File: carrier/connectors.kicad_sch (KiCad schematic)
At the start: 1 part, among them J11 Conn_02x05_Top_Bottom

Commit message: Fix: relinked footprints
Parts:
- added J12: Conn_02x40_Odd_Even, symbol Connector_Generic:Conn_02x40_Odd_Even
- J11: footprint (none) -> Connector_PinHeader_2.54mm:PinHeader_2x05_P2.54mm_Vertical
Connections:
- new net +5v: J12.10 (Pin_10), J12.12 (Pin_12), J12.14 (Pin_14), J12.16 (Pin_16), J12.18 (Pin_18), J12.2 (Pin_2), J12.20 (Pin_20), J12.22 (Pin_22), J12.24 (Pin_24), J12.26 (Pin_26), J12.28 (Pin_28), J12.30 (Pin_30), J12.32 (Pin_32), J12.34 (Pin_34), J12.36 (Pin_36), J12.38 (Pin_38), J12.4 (Pin_4), J12.40 (Pin_40), J12.42 (Pin_42), J12.44 (Pin_44), J12.46 (Pin_46), J12.48 (Pin_48), J12.50 (Pin_50), J12.52 (Pin_52), J12.54 (Pin_54), J12.56 (Pin_56), J12.58 (Pin_58), J12.6 (Pin_6), J12.60 (Pin_60), J12.62 (Pin_62), J12.64 (Pin_64), J12.66 (Pin_66), J12.68 (Pin_68), J12.70 (Pin_70), J12.72 (Pin_72), J12.74 (Pin_74), J12.8 (Pin_8)
- new net GND: J12.11 (Pin_11), J12.13 (Pin_13), J12.15 (Pin_15), J12.17 (Pin_17), J12.19 (Pin_19), J12.21 (Pin_21), J12.23 (Pin_23), J12.25 (Pin_25), J12.27 (Pin_27), J12.29 (Pin_29), J12.31 (Pin_31), J12.33 (Pin_33), J12.35 (Pin_35), J12.37 (Pin_37), J12.39 (Pin_39), J12.41 (Pin_41), J12.43 (Pin_43), J12.45 (Pin_45), J12.47 (Pin_47), J12.49 (Pin_49), J12.51 (Pin_51), J12.53 (Pin_53), J12.55 (Pin_55), J12.57 (Pin_57), J12.59 (Pin_59), J12.61 (Pin_61), J12.63 (Pin_63), J12.65 (Pin_65), J12.67 (Pin_67), J12.69 (Pin_69), J12.71 (Pin_71), J12.73 (Pin_73), J12.75 (Pin_75), J12.9 (Pin_9)
- new net RX: J12.1 (Pin_1), J12.3 (Pin_3)
- new net TX: J12.5 (Pin_5), J12.7 (Pin_7)
- no-connect marks 0 -> 5
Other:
- moved on the sheet: J11

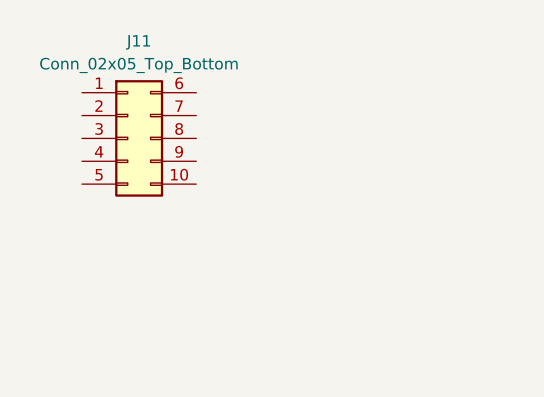
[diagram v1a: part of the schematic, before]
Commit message: Feat: begun work on carrier pcb and imported NGFF m.2 library
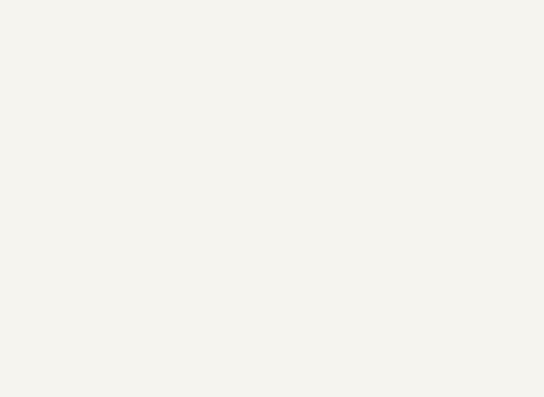
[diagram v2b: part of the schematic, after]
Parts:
- removed J11: Conn_02x05_Top_Bottom, Connector_PinHeader_2.54mm:PinHeader_2x05_P2.54mm_Vertical, symbol Connector_Generic:Conn_02x05_Top_Bottom
- J12: footprint (none) -> M.2:NGFF_A
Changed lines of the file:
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@@
     (effects (font (size 1.27 1.27)) (justify left))
-  )
-  (symbol (lib_id "Connector_Generic:Conn_02x05_Top_Bottom") (at 44.45 59.69 0) (unit 1)
-    (in_bom yes) (on_board yes) (dnp no) (fields_autoplaced)
-    (property "Reference" "J11" (at 45.72 48.895 0)
-      (effects (font (size 1.27 1.27)))
-    )
-    (property "Value" "Conn_02x05_Top_Bottom" (at 45.72 51.435 0)
-      (effects (font (size 1.27 1.27)))
-    )
-    (property "Footprint" "Connector_PinHeader_2.54mm:PinHeader_2x05_P2.54mm_Vertical" (at 44.45 59.69 0)
-      (effects (font (size 1.27 1.27)) hide)
-    )
-    (property "Datasheet" "~" (at 44.45 59.69 0)
-      (effects (font (size 1.27 1.27)) hide)
-    )
-    (pin "1")
-    (pin "10")
-    (pin "2")
-    (pin "3")
-    (pin "4")
-    (pin "5")
-    (pin "6")
-    (pin "7")
-    (pin "8")
-    (pin "9")
-    (instances
-      (project "carrier"
-        (path "/4b1cea9d-93bc-4380-88c3-ede99bb53de2/af6c5568-d2e2-4612-83c1-6e53a7c32d99"
-          (reference "J11") (unit 1)
-        )
-      )
-    )
   )
   (symbol (lib_id "Connector_Generic:Conn_02x40_Odd_Even") (at 111.76 102.235 0) (unit 1)
@@
       (effects (font (size 1.27 1.27)))
     )
-    (property "Footprint" "" (at 111.76 102.235 0)
+    (property "Footprint" "M.2:NGFF_A" (at 111.76 102.235 0)
       (effects (font (size 1.27 1.27)) hide)
     )

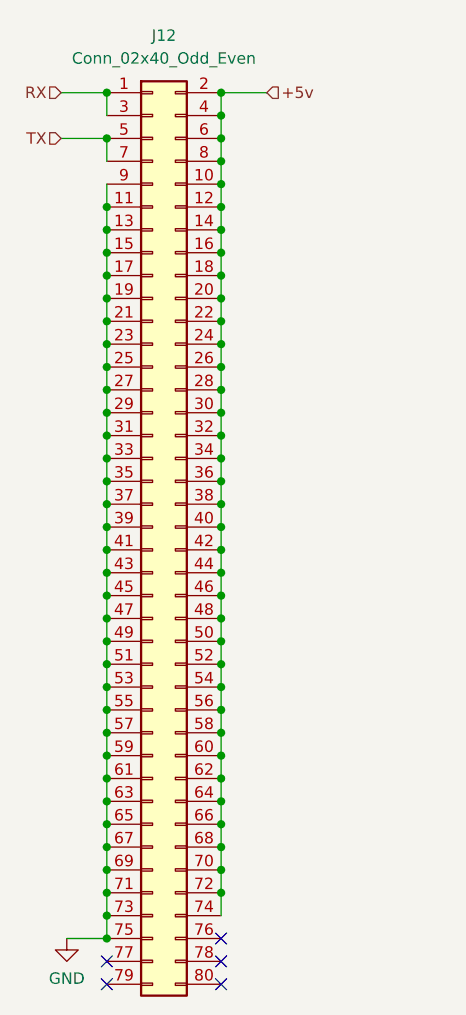
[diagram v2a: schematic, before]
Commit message: Feat: imported m.2 connector and more work on carrier board
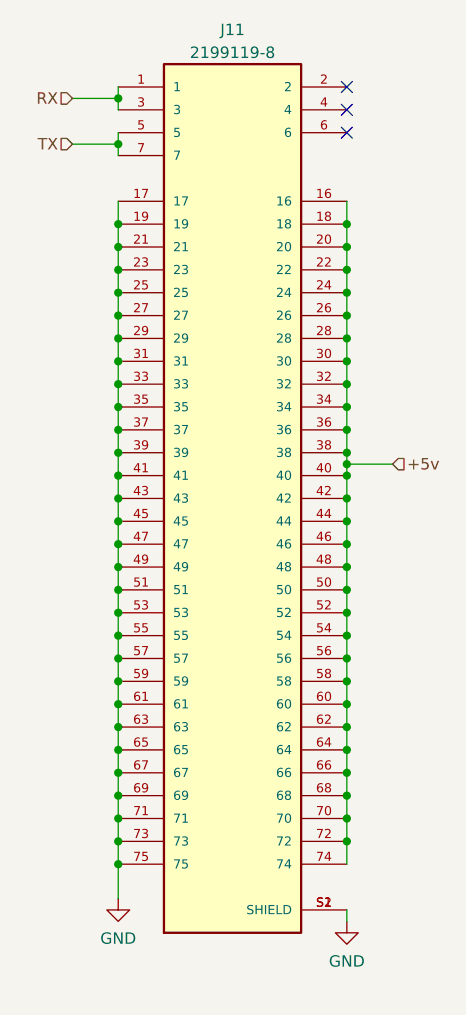
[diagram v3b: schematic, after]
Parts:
- removed J12: Conn_02x40_Odd_Even, M.2:NGFF_A, symbol Connector_Generic:Conn_02x40_Odd_Even
- added J11: 2199119-8, M.2_Connector:TE_2199119-8, symbol M.2_Connector:2199119-8
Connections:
- net +5v: now also J11.16, J11.18, J11.20, J11.22, J11.24, J11.26, J11.28, J11.30, J11.32, J11.34, J11.36, J11.38, J11.40, J11.42, J11.44, J11.46, J11.48, J11.50, J11.52, J11.54, J11.56, J11.58, J11.60, J11.62, J11.64, J11.66, J11.68, J11.70, J11.72, J11.74
- net GND: now also J11.17, J11.19, J11.21, J11.23, J11.25, J11.27, J11.29, J11.31, J11.33, J11.35, J11.37, J11.39, J11.41, J11.43, J11.45, J11.47, J11.49, J11.51, J11.53, J11.55, J11.57, J11.59, J11.61, J11.63, J11.65, J11.67, J11.69, J11.71, J11.73, J11.75, J11.S1 (SHIELD), J11.S2 (SHIELD)
- net RX: now also J11.1, J11.3
- net TX: now also J11.5, J11.7
- no-connect marks 5 -> 3

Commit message: Feat: organized PCB file, preparing for layout and routing.
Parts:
- added J12: Conn_01x04, symbol Connector_Generic:Conn_01x04
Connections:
- net GND: now also J12.2 (Pin_2), J12.4 (Pin_4)
- net RX: now also J12.1 (Pin_1)
- net TX: now also J12.3 (Pin_3)
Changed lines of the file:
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@@
+    (stroke (width 0) (type default))
+  )
+  (wire (pts (xy 163.83 106.68) (xy 170.18 106.68))
     (stroke (width 0) (type default))
   )
@@
     (stroke (width 0) (type default))
   )
+  (wire (pts (xy 163.83 111.76) (xy 170.18 111.76))
+    (stroke (width 0) (type default))
+  )
   (wire (pts (xy 107.95 78.74) (xy 107.95 81.28))
     (stroke (width 0) (type default))
@@
   )
   (hierarchical_label "TX" (shape input) (at 102.87 59.69 180) (fields_autoplaced)
+    (effects (font (size 1.27 1.27)) (justify right))
+  )
+  (hierarchical_label "TX" (shape input) (at 170.18 109.22 180) (fields_autoplaced)
+    (effects (font (size 1.27 1.27)) (justify right))
+  )
+  (hierarchical_label "RX" (shape input) (at 170.18 104.14 180) (fields_autoplaced)
     (effects (font (size 1.27 1.27)) (justify right))
   )
@@
     )
   )
+  (symbol (lib_id "power:GND") (at 163.83 111.76 0) (unit 1)
+    (in_bom yes) (on_board yes) (dnp no)
+    (property "Reference" "#PWR064" (at 163.83 118.11 0)
+      (effects (font (size 1.27 1.27)) hide)
+    )
+    (property "Value" "GND" (at 160.02 113.03 0)
+      (effects (font (size 1.27 1.27)))
+    )
+    (property "Footprint" "" (at 163.83 111.76 0)
+      (effects (font (size 1.27 1.27)) hide)
+    )
+    (property "Datasheet" "" (at 163.83 111.76 0)
+      (effects (font (size 1.27 1.27)) hide)
+    )
+    (pin "1")
+    (instances
+      (project "carrier"
+        (path "/4b1cea9d-93bc-4380-88c3-ede99bb53de2/af6c5568-d2e2-4612-83c1-6e53a7c32d99"
+          (reference "#PWR064") (unit 1)
+        )
+      )
+    )
+  )
   (symbol (lib_id "power:GND") (at 107.95 143.51 0) (unit 1)
     (in_bom yes) (on_board yes) (dnp no) (fields_autoplaced)
@@
     )
   )
+  (symbol (lib_id "Connector_Generic:Conn_01x04") (at 175.26 106.68 0) (unit 1)
+    (in_bom yes) (on_board yes) (dnp no) (fields_autoplaced)
+    (property "Reference" "J12" (at 177.8 107.315 0)
+      (effects (font (size 1.27 1.27)) (justify left))
+    )
+    (property "Value" "Conn_01x04" (at 177.8 109.855 0)
+      (effects (font (size 1.27 1.27)) (justify left))
+    )
+    (property "Footprint" "" (at 175.26 106.68 0)
+      (effects (font (size 1.27 1.27)) hide)
+    )
+    (property "Datasheet" "~" (at 175.26 106.68 0)
+      (effects (font (size 1.27 1.27)) hide)
+    )
+    (pin "1")
+    (pin "2")
+    (pin "3")
+    (pin "4")
+    (instances
+      (project "carrier"
+        (path "/4b1cea9d-93bc-4380-88c3-ede99bb53de2/af6c5568-d2e2-4612-83c1-6e53a7c32d99"
+          (reference "J12") (unit 1)
+        )
+      )
+    )
+  )
   (symbol (lib_id "power:GND") (at 133.35 146.05 0) (unit 1)
     (in_bom yes) (on_board yes) (dnp no) (fields_autoplaced)
@@
         )
       )
+    )
+  )
+  (symbol (lib_id "power:GND") (at 163.83 106.68 0) (unit 1)
+    (in_bom yes) (on_board yes) (dnp no)
+    (property "Reference" "#PWR073" (at 163.83 113.03 0)
+      (effects (font (size 1.27 1.27)) hide)
+    )
+    (property "Value" "GND" (at 160.02 107.95 0)
+      (effects (font (size 1.27 1.27)))
+    )
+    (property "Footprint" "" (at 163.83 106.68 0)
+      (effects (font (size 1.27 1.27)) hide)
+    )
+    (property "Datasheet" "" (at 163.83 106.68 0)
+      (effects (font (size 1.27 1.27)) hide)
+    )
+    (pin "1")
+    (instances
+      (project "carrier"
+        (path "/4b1cea9d-93bc-4380-88c3-ede99bb53de2/af6c5568-d2e2-4612-83c1-6e53a7c32d99"
+          (reference "#PWR073") (unit 1)
+        )
+      )

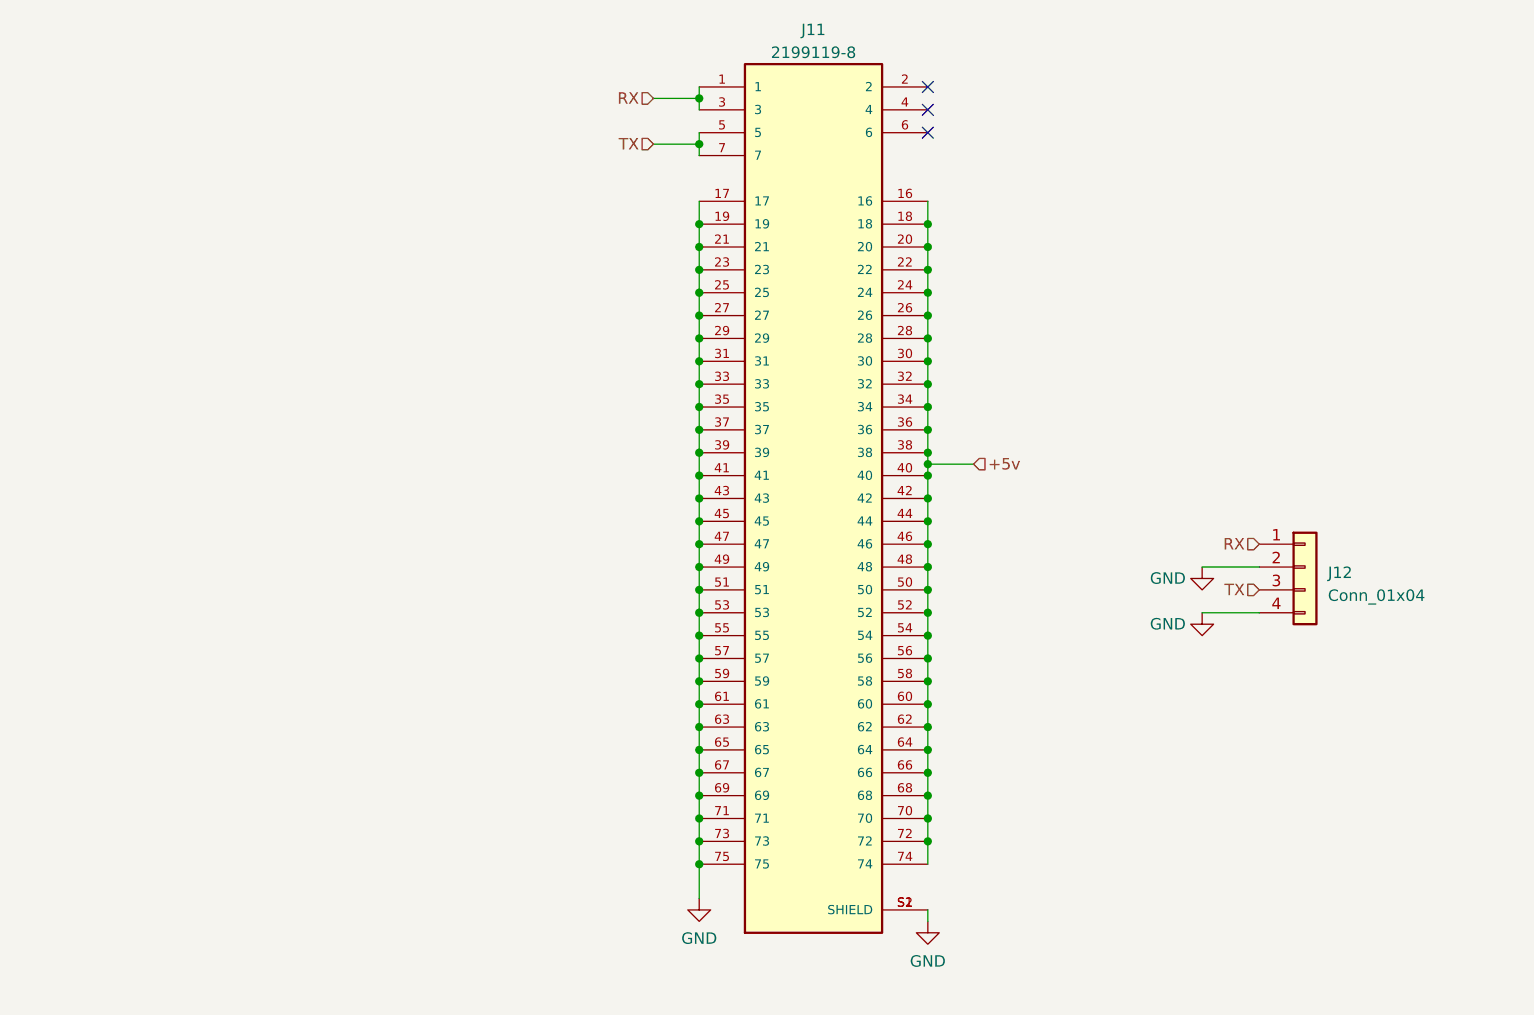
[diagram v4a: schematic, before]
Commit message: Feat: begun work on finalizing PCB layout
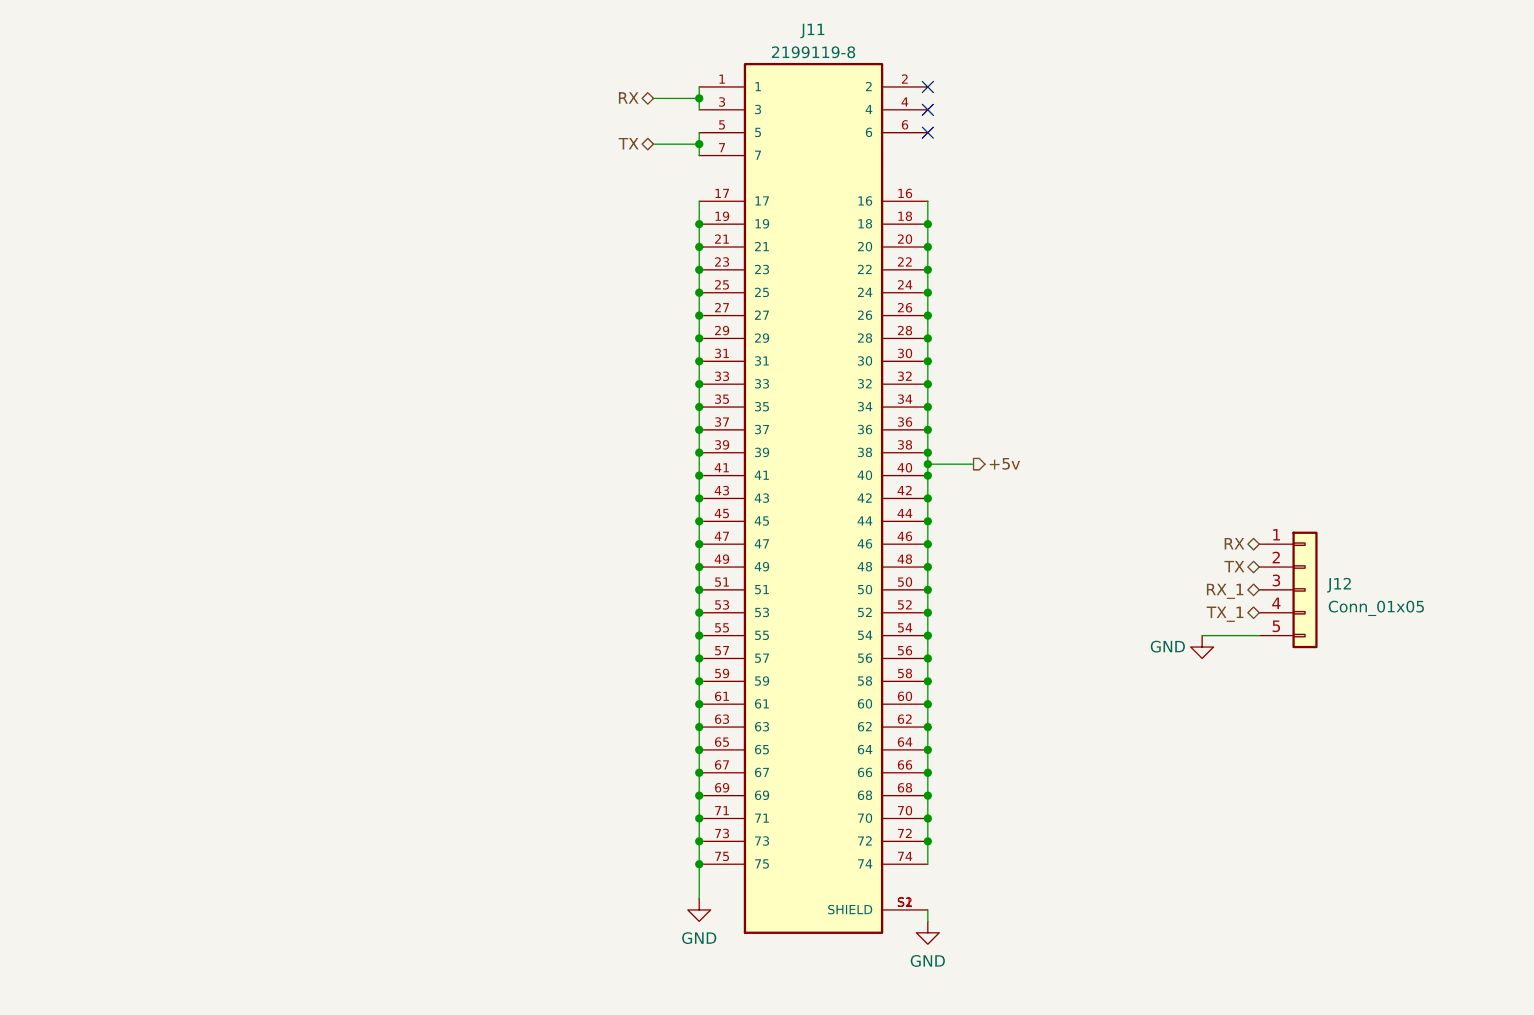
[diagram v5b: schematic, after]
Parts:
- removed J12: Conn_01x04, symbol Connector_Generic:Conn_01x04
- added J12: Conn_01x05, Connector_Molex:Molex_PicoBlade_53048-0510_1x05_P1.25mm_Horizontal, symbol Connector_Generic:Conn_01x05
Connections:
- net GND: now also J12.5 (Pin_5)
- net RX: now also J12.1 (Pin_1)
- net TX: now also J12.2 (Pin_2)
- new net RX_1: J12.3 (Pin_3)
- new net TX_1: J12.4 (Pin_4)
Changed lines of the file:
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@@
-    (stroke (width 0) (type default))
-  )
-  (wire (pts (xy 163.83 106.68) (xy 170.18 106.68))
     (stroke (width 0) (type default))
   )
@@
     (stroke (width 0) (type default))
   )
-  (wire (pts (xy 163.83 111.76) (xy 170.18 111.76))
+  (wire (pts (xy 163.83 114.3) (xy 170.18 114.3))
     (stroke (width 0) (type default))
   )
@@
     (stroke (width 0) (type default))
   )
-  (hierarchical_label "RX" (shape input) (at 102.87 54.61 180) (fields_autoplaced)
-    (effects (font (size 1.27 1.27)) (justify right))
-  )
-  (hierarchical_label "TX" (shape input) (at 102.87 59.69 180) (fields_autoplaced)
-    (effects (font (size 1.27 1.27)) (justify right))
-  )
-  (hierarchical_label "TX" (shape input) (at 170.18 109.22 180) (fields_autoplaced)
-    (effects (font (size 1.27 1.27)) (justify right))
-  )
-  (hierarchical_label "RX" (shape input) (at 170.18 104.14 180) (fields_autoplaced)
-    (effects (font (size 1.27 1.27)) (justify right))
-  )
-  (hierarchical_label "+5v" (shape input) (at 138.43 95.25 0) (fields_autoplaced)
+  (hierarchical_label "RX" (shape bidirectional) (at 102.87 54.61 180) (fields_autoplaced)
+    (effects (font (size 1.27 1.27)) (justify right))
+  )
+  (hierarchical_label "TX" (shape bidirectional) (at 102.87 59.69 180) (fields_autoplaced)
+    (effects (font (size 1.27 1.27)) (justify right))
+  )
+  (hierarchical_label "TX" (shape bidirectional) (at 170.18 106.68 180) (fields_autoplaced)
+    (effects (font (size 1.27 1.27)) (justify right))
+  )
+  (hierarchical_label "TX_1" (shape bidirectional) (at 170.18 111.76 180) (fields_autoplaced)
+    (effects (font (size 1.27 1.27)) (justify right))
+  )
+  (hierarchical_label "RX_1" (shape bidirectional) (at 170.18 109.22 180) (fields_autoplaced)
+    (effects (font (size 1.27 1.27)) (justify right))
+  )
+  (hierarchical_label "RX" (shape bidirectional) (at 170.18 104.14 180) (fields_autoplaced)
+    (effects (font (size 1.27 1.27)) (justify right))
+  )
+  (hierarchical_label "+5v" (shape output) (at 138.43 95.25 0) (fields_autoplaced)
     (effects (font (size 1.27 1.27)) (justify left))
   )
@@
     )
   )
-  (symbol (lib_id "power:GND") (at 163.83 111.76 0) (unit 1)
+  (symbol (lib_id "Connector_Generic:Conn_01x05") (at 175.26 109.22 0) (unit 1)
+    (in_bom yes) (on_board yes) (dnp no) (fields_autoplaced)
+    (property "Reference" "J12" (at 177.8 108.585 0)
+      (effects (font (size 1.27 1.27)) (justify left))
+    )
+    (property "Value" "Conn_01x05" (at 177.8 111.125 0)
+      (effects (font (size 1.27 1.27)) (justify left))
+    )
+    (property "Footprint" "Connector_Molex:Molex_PicoBlade_53048-0510_1x05_P1.25mm_Horizontal" (at 175.26 109.22 0)
+      (effects (font (size 1.27 1.27)) hide)
+    )
+    (property "Datasheet" "~" (at 175.26 109.22 0)
+      (effects (font (size 1.27 1.27)) hide)
+    )
+    (pin "1")
+    (pin "2")
+    (pin "3")
+    (pin "4")
+    (pin "5")
+    (instances
+      (project "carrier"
+        (path "/4b1cea9d-93bc-4380-88c3-ede99bb53de2/af6c5568-d2e2-4612-83c1-6e53a7c32d99"
+          (reference "J12") (unit 1)
+        )
+      )
+    )
+  )
+  (symbol (lib_id "power:GND") (at 163.83 114.3 0) (unit 1)
     (in_bom yes) (on_board yes) (dnp no)
-    (property "Reference" "#PWR064" (at 163.83 118.11 0)
-      (effects (font (size 1.27 1.27)) hide)
-    )
-    (property "Value" "GND" (at 160.02 113.03 0)
+    (property "Reference" "#PWR064" (at 163.83 120.65 0)
+      (effects (font (size 1.27 1.27)) hide)
+    )
+    (property "Value" "GND" (at 160.02 115.57 0)
       (effects (font (size 1.27 1.27)))
     )
-    (property "Footprint" "" (at 163.83 111.76 0)
-      (effects (font (size 1.27 1.27)) hide)
-    )
-    (property "Datasheet" "" (at 163.83 111.76 0)
+    (property "Footprint" "" (at 163.83 114.3 0)
+      (effects (font (size 1.27 1.27)) hide)
+    )
+    (property "Datasheet" "" (at 163.83 114.3 0)
       (effects (font (size 1.27 1.27)) hide)
     )
@@
     )
   )
-  (symbol (lib_id "Connector_Generic:Conn_01x04") (at 175.26 106.68 0) (unit 1)
-    (in_bom yes) (on_board yes) (dnp no) (fields_autoplaced)
-    (property "Reference" "J12" (at 177.8 107.315 0)
-      (effects (font (size 1.27 1.27)) (justify left))
-    )
-    (property "Value" "Conn_01x04" (at 177.8 109.855 0)
-      (effects (font (size 1.27 1.27)) (justify left))
-    )
-    (property "Footprint" "" (at 175.26 106.68 0)
-      (effects (font (size 1.27 1.27)) hide)
-    )
-    (property "Datasheet" "~" (at 175.26 106.68 0)
-      (effects (font (size 1.27 1.27)) hide)
-    )
-    (pin "1")
-    (pin "2")
-    (pin "3")
-    (pin "4")
-    (instances
-      (project "carrier"
-        (path "/4b1cea9d-93bc-4380-88c3-ede99bb53de2/af6c5568-d2e2-4612-83c1-6e53a7c32d99"
-          (reference "J12") (unit 1)
-        )
-      )
-    )
-  )
   (symbol (lib_id "power:GND") (at 133.35 146.05 0) (unit 1)
     (in_bom yes) (on_board yes) (dnp no) (fields_autoplaced)
@@
         )
       )
-    )
-  )
-  (symbol (lib_id "power:GND") (at 163.83 106.68 0) (unit 1)
-    (in_bom yes) (on_board yes) (dnp no)
-    (property "Reference" "#PWR073" (at 163.83 113.03 0)
-      (effects (font (size 1.27 1.27)) hide)
-    )
-    (property "Value" "GND" (at 160.02 107.95 0)
-      (effects (font (size 1.27 1.27)))
-    )
-    (property "Footprint" "" (at 163.83 106.68 0)
-      (effects (font (size 1.27 1.27)) hide)
-    )
-    (property "Datasheet" "" (at 163.83 106.68 0)
-      (effects (font (size 1.27 1.27)) hide)
-    )
-    (pin "1")
-    (instances
-      (project "carrier"
-        (path "/4b1cea9d-93bc-4380-88c3-ede99bb53de2/af6c5568-d2e2-4612-83c1-6e53a7c32d99"
-          (reference "#PWR073") (unit 1)
-        )
-      )

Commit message: Feat: power line routing, marked down necessary revisions, rerouted i2c
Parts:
- J12: footprint Connector_Molex:Molex_PicoBlade_53048-0510_1x05_P1.25mm_Horizontal -> Connector_Molex:Molex_PicoBlade_53047-0510_1x05_P1.25mm_Vertical
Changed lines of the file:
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@@
       (effects (font (size 1.27 1.27)) (justify left))
     )
-    (property "Footprint" "Connector_Molex:Molex_PicoBlade_53048-0510_1x05_P1.25mm_Horizontal" (at 175.26 109.22 0)
+    (property "Footprint" "Connector_Molex:Molex_PicoBlade_53047-0510_1x05_P1.25mm_Vertical" (at 175.26 109.22 0)
       (effects (font (size 1.27 1.27)) hide)
     )
